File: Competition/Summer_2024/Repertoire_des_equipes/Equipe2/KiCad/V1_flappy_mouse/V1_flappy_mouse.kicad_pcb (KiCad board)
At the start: 2 copper layers, 1 part

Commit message: Push pcb
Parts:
- removed REF**: Touchpad_spiral, Librairie_touchpad:Touchpad_spiral
- added D301: TRIG LED, LED_THT:LED_D5.0mm_IRGrey, F.Cu at (204.6, 30.4)
- added D302: PWR LED, LED_THT:LED_D5.0mm_IRGrey, F.Cu at (212.3, 30.0)
- added J201: Conn_01x05_no_connect(SPI), Connector_PinSocket_2.54mm:PinSocket_1x05_P2.54mm_Vertical, F.Cu at (149.0, 137.1)
- added J202: Conn_accelerometer_I2C, Connector_PinSocket_2.54mm:PinSocket_1x07_P2.54mm_Vertical, F.Cu at (162.0, 139.6)
- added J203: Conn_Module_SD, Connector_PinSocket_2.54mm:PinSocket_1x06_P2.54mm_Vertical, F.Cu at (149.2, 94.9)
- added J301: ESP_GAUCHE, Connector_PinSocket_2.54mm:PinSocket_1x22_P2.54mm_Vertical, F.Cu at (145.2, 148.1)
- added J302: ESP_DROIT, Connector_PinSocket_2.54mm:PinSocket_1x22_P2.54mm_Vertical, F.Cu at (119.8, 148.1)
- added J304: Conn_01x08_Pin, Connector_PinSocket_2.54mm:PinSocket_1x08_P2.54mm_Vertical, F.Cu at (213.7, 42.4)
- added SW201: JS102011JAQN, Button_Switch_SMD:SW_SPDT_CK_JS102011SAQN, F.Cu at (155.9, 147.6)
- added TP201: Touchpad_click_droit, Librairie_touchpad:Touchpad_biz_rect, F.Cu at (154.0, 66.6)
- added TP202: Touchpad_scroll1, Librairie_touchpad:Touchpad_slider, F.Cu at (138.5, 74.0)
- added TP203: Touchpad_scroll2, Librairie_touchpad:Touchpad_slider, F.Cu at (138.5, 66.1)
- added TP204: Touchpad_scroll3, Librairie_touchpad:Touchpad_slider, F.Cu at (138.5, 58.1)
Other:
- board outline added: 65 x 95 mm

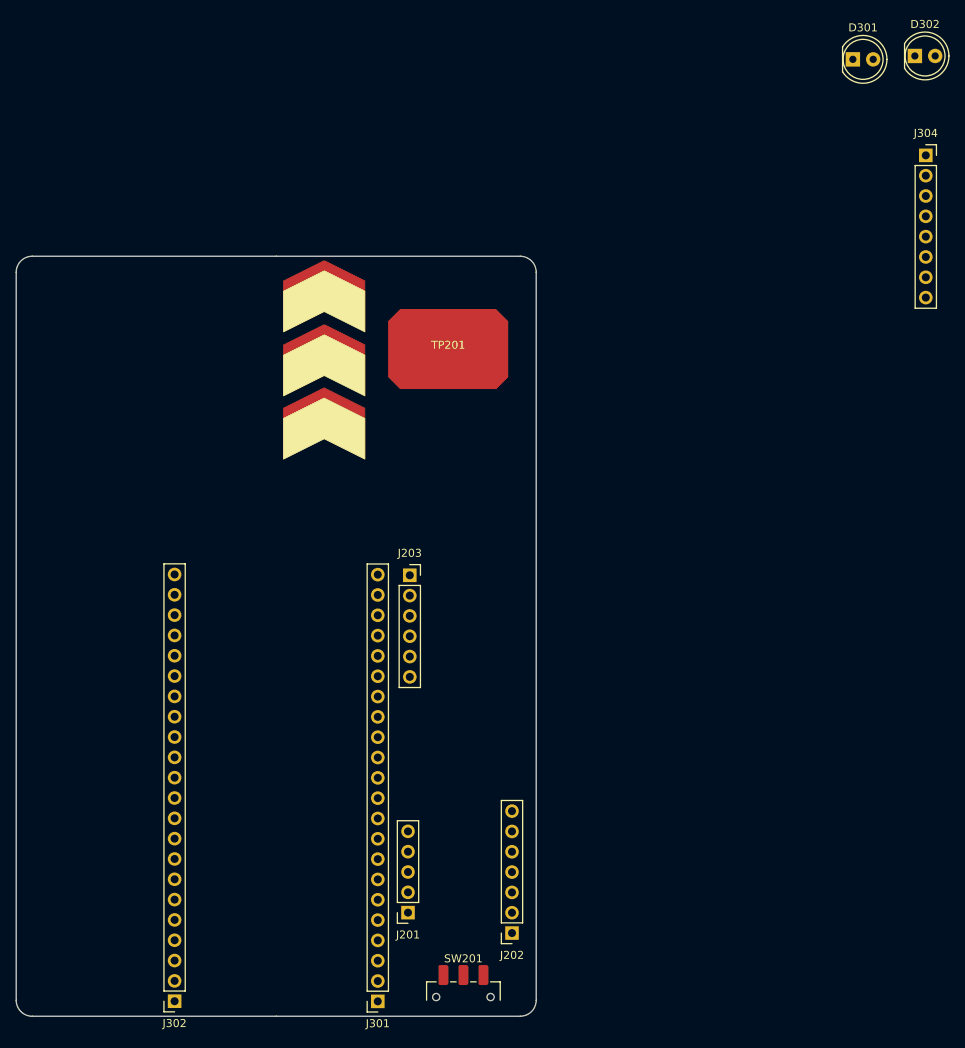
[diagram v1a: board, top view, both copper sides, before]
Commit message: add the component on the PCB
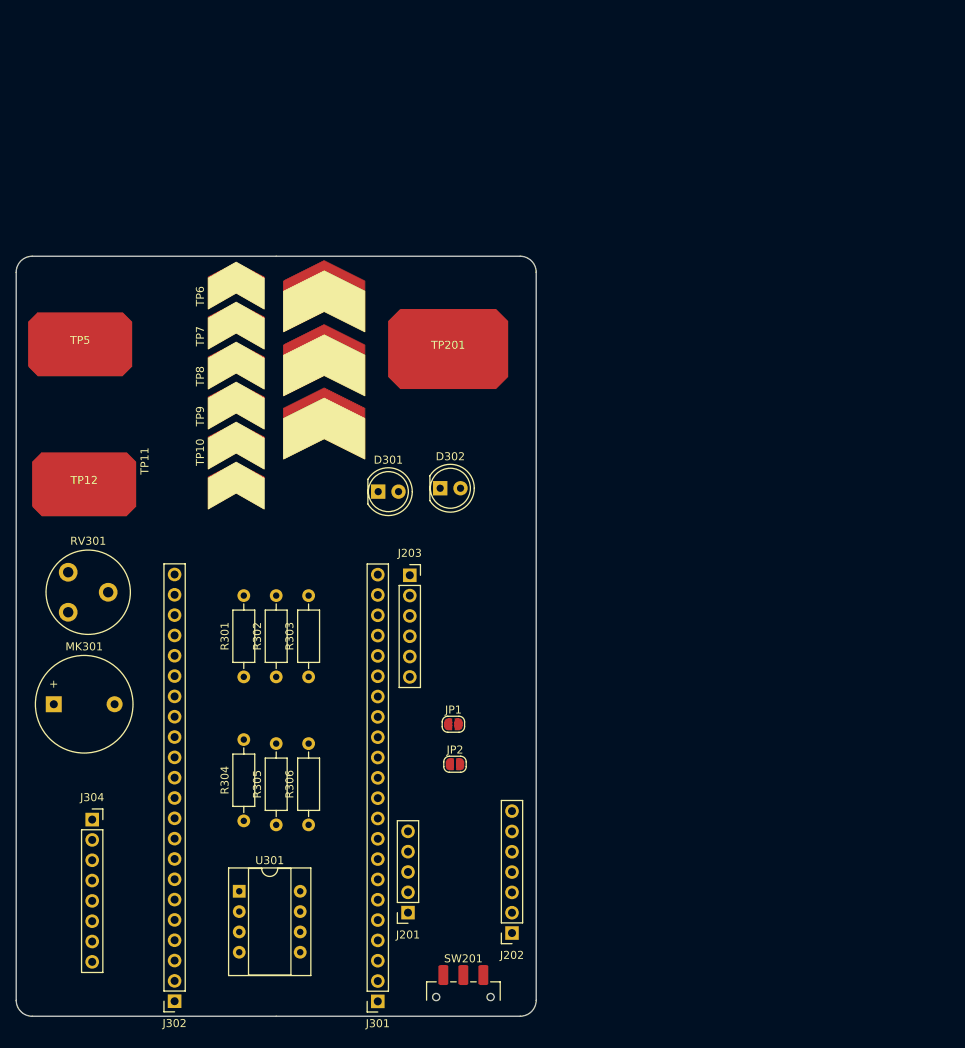
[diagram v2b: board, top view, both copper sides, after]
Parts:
- added JP1: SolderJumper_AOUT, Jumper:SolderJumper-2_P1.3mm_Open_RoundedPad1.0x1.5mm, F.Cu at (154.7, 113.5)
- added JP2: SolderJumper_DOUT, Jumper:SolderJumper-2_P1.3mm_Open_RoundedPad1.0x1.5mm, F.Cu at (154.8, 118.5)
- added MK301: Mic, Buzzer_Beeper:Buzzer_12x9.5RM7.6, F.Cu at (104.7, 111.0)
- added R301: 100K, Resistor_THT:R_Axial_DIN0207_L6.3mm_D2.5mm_P10.16mm_Horizontal, F.Cu at (128.4, 107.6)
- added R302: 100K, Resistor_THT:R_Axial_DIN0207_L6.3mm_D2.5mm_P10.16mm_Horizontal, F.Cu at (132.5, 107.6)
- added R303: 150, Resistor_THT:R_Axial_DIN0207_L6.3mm_D2.5mm_P10.16mm_Horizontal, F.Cu at (136.6, 107.6)
- added R304: 1K, Resistor_THT:R_Axial_DIN0207_L6.3mm_D2.5mm_P10.16mm_Horizontal, F.Cu at (128.4, 125.6)
- added R305: 1K, Resistor_THT:R_Axial_DIN0207_L6.3mm_D2.5mm_P10.16mm_Horizontal, F.Cu at (132.5, 126.1)
- added R306: 10K, Resistor_THT:R_Axial_DIN0207_L6.3mm_D2.5mm_P10.16mm_Horizontal, F.Cu at (136.6, 126.1)
- added RV301: 10K, Potentiometer_THT:Potentiometer_Piher_PT-10-V05_Vertical, F.Cu at (106.5, 99.5)
- added TP10: Touchpad_scroll8, Librairie_touchpad:Touchpad_slider_smaller, F.Cu at (127.5, 75.6)
- added TP11: Touchpad_scroll9, Librairie_touchpad:Touchpad_slider_smaller, F.Cu at (127.5, 80.6)
- added TP12: Touchpad_stopMouseMotion, Librairie_touchpad:Touchpad_biz_rect_smaller, F.Cu at (108.5, 83.5)
- added TP5: Touchpad_click_gauche, Librairie_touchpad:Touchpad_biz_rect_smaller, F.Cu at (108.0, 66.0)
- added TP6: Touchpad_scroll4, Librairie_touchpad:Touchpad_slider_smaller, F.Cu at (127.5, 55.6)
- added TP7: Touchpad_scroll5, Librairie_touchpad:Touchpad_slider_smaller, F.Cu at (127.5, 60.6)
- added TP8: Touchpad_scroll6, Librairie_touchpad:Touchpad_slider_smaller, F.Cu at (127.5, 65.6)
- added TP9: Touchpad_scroll7, Librairie_touchpad:Touchpad_slider_smaller, F.Cu at (127.5, 70.6)
- added U301: LM393, Package_DIP:CERDIP-8_W7.62mm_SideBrazed_Socket, F.Cu at (127.9, 134.4)
- J304: value Conn_01x08_Pin -> Conn_TFT_display
- moved J304 133.2 mm to (109.5, 125.4)
- moved D301 80.3 mm to (145.2, 84.4)
- moved D302 80.3 mm to (153.0, 84.0)
